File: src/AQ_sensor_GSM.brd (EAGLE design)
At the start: 110 x 64 mm, 51 parts, among them IC2 MCP73831/OT, J1 F-1X03-SIP-100-32, SW1 PCM12SMTR, SW2 PCM12SMTR, U2 TEXAS_INSTRUMENTS_SN74HC125TE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, U3 TEXAS_INSTRUMENTS_LM1117IMP-3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, U4 ESP8266-12E/ESP-12E, U5 CH340G, X1 53048-08, X2 SIMLOCK-C707_10M006_512_2, X4 50 Ohms

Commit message: Layout Update 2
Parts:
- moved POWER 107.0 mm to (9.54, 62.5)
- moved R14 103.9 mm to (7.71, 54.3), turned to 90 degrees
- moved C3 95.1 mm to (34.0, 54.8), turned to 90 degrees
- moved MICRO_USB 93.4 mm to (16.4, 60.0), turned to 180 degrees
- moved C2 87.8 mm to (34.0, 49.3), turned to 90 degrees
- moved R5 79.9 mm to (30.1, 14.7)
- moved J1 79.1 mm to (36.4, 14.2)
- moved R2 75.8 mm to (9.30, 59.5), turned to 270 degrees
- moved SW1 75.3 mm to (38.5, 59.0), turned to 90 degrees
- moved X1 61.1 mm to (35.5, 37.0), turned to 270 degrees
- moved C1 51.2 mm to (48.0, 34.4)
- moved Y1 35.1 mm to (30.2, 51.7), turned to 90 degrees
- moved U5 31.7 mm to (18.3, 51.4), turned to 270 degrees
- moved PMS 26.0 mm to (32.8, 28.0), turned to 270 degrees
- moved R4 23.8 mm to (30.2, 21.8)
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
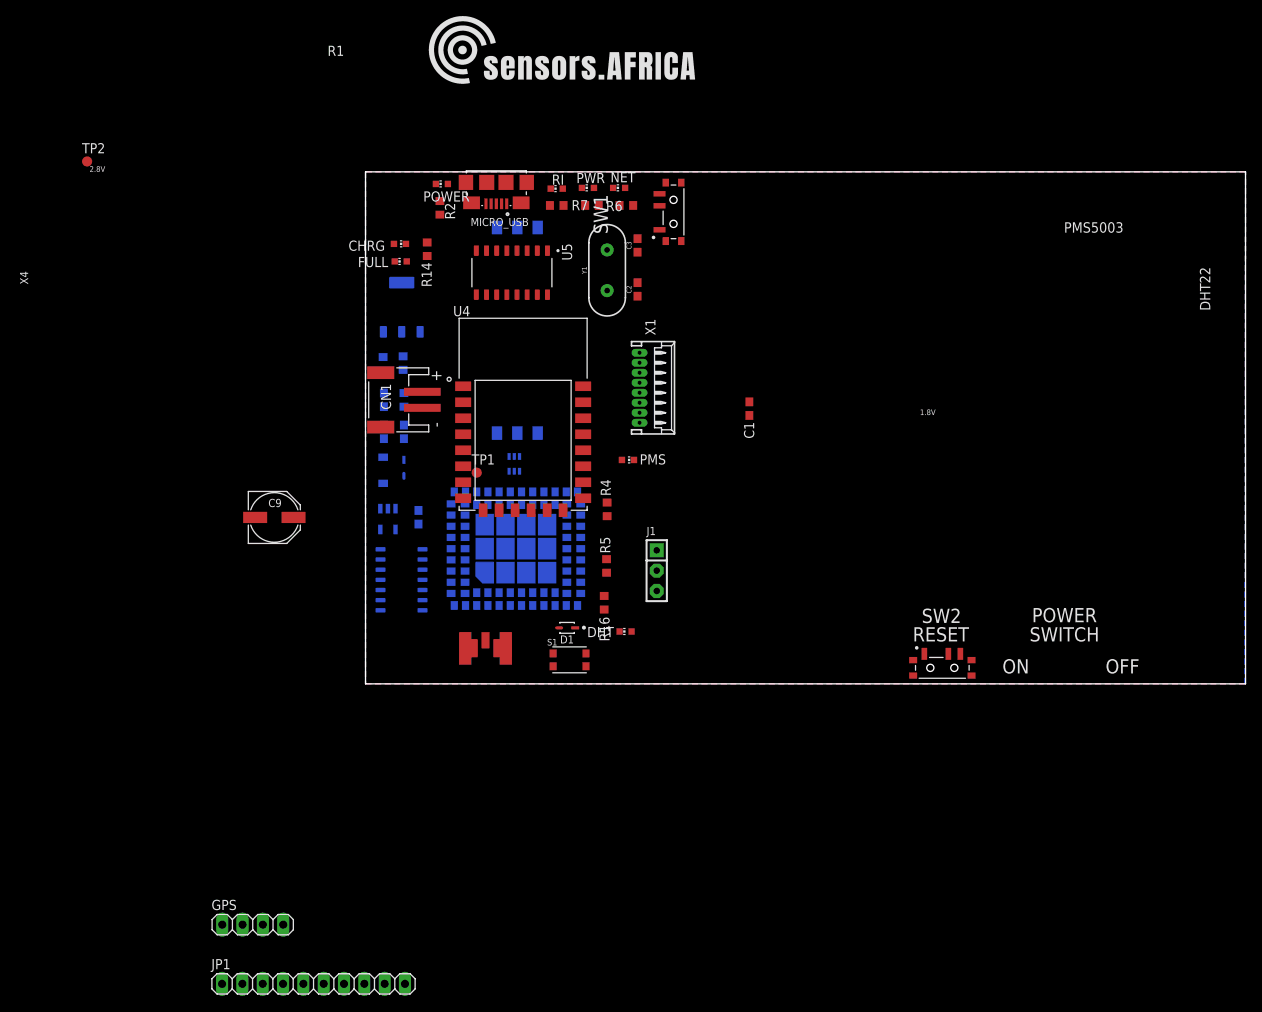
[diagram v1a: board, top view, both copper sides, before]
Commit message: PCB Resized
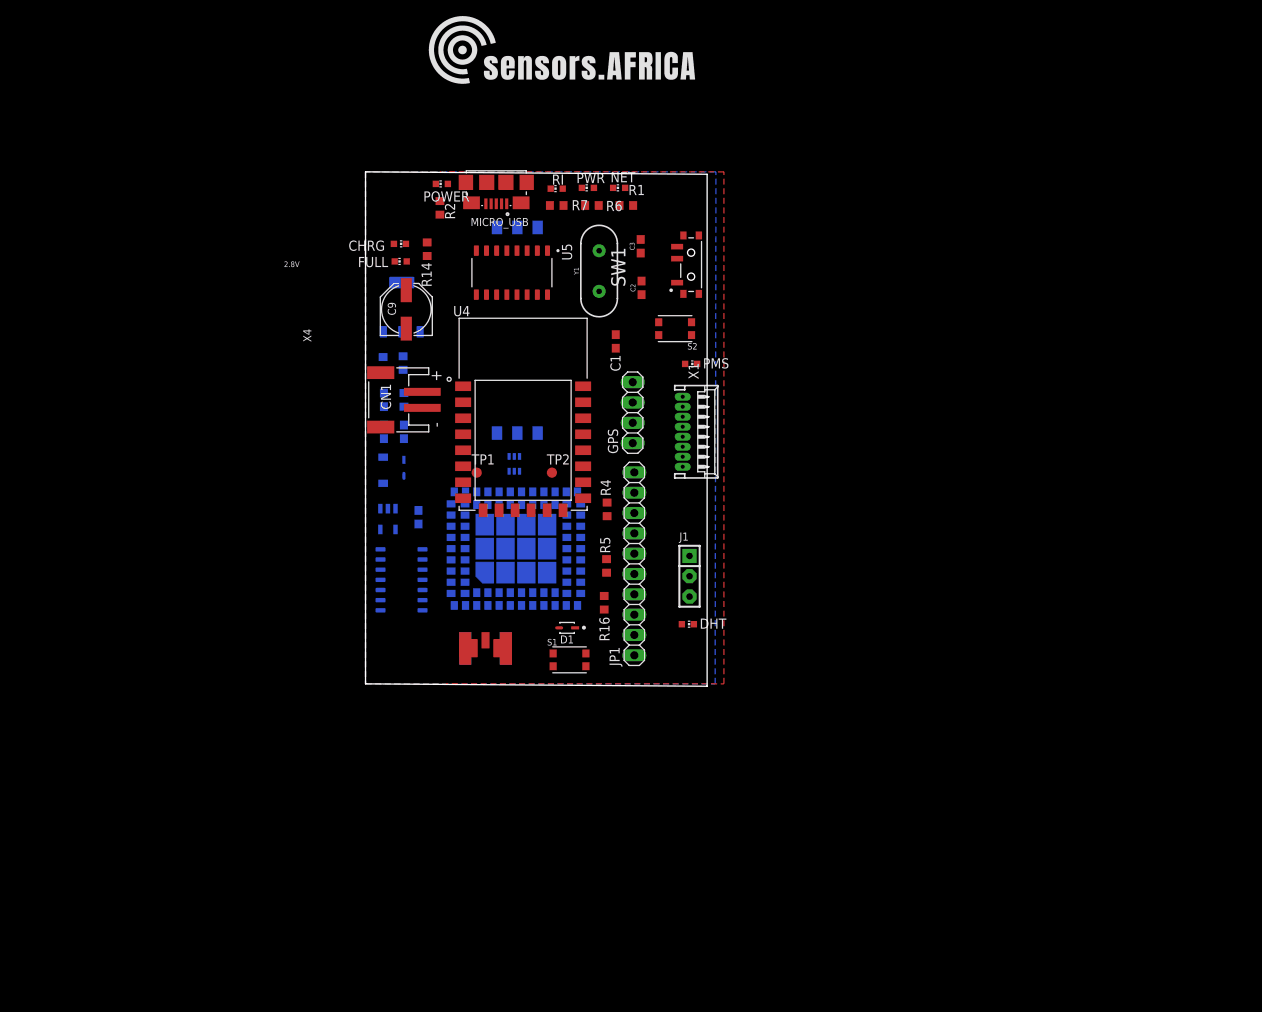
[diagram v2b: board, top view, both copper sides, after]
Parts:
- removed SW2: PCM12SMTR, AQ_sensor_GSM:SW_PCM12SMTR
- added S2: KMR621NGLFS, AQ_sensor_GSM:SW_KMR621NGLFS
- moved GPS 79.7 mm to (33.4, 33.9), turned to 90 degrees
- moved TP2 69.9 mm to (23.3, 26.4)
- moved JP1 66.1 mm to (33.6, 15.0), turned to 90 degrees
- moved C9 30.8 mm to (5.10, 46.8), turned to 90 degrees
- moved C1 18.7 mm to (31.3, 42.8)
- moved PMS 14.4 mm to (40.7, 40.0)
- moved DHT 7.84 mm to (40.3, 7.46), turned to 270 degrees
- moved X1 7.71 mm to (40.9, 31.5)
- moved SW1 6.96 mm to (40.7, 52.4)
- moved J1 4.16 mm to (40.5, 13.4)
- moved Y1 1.00 mm to (29.2, 51.6)
- moved C2 0.54 mm to (34.5, 49.5)
- moved C3 0.41 mm to (34.4, 54.7)
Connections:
- net ESP_RST: now also S2.1_1, S2.1_2; no longer SW2.2
- net GND: now also S2.2_1, S2.2_2; no longer SW2.1, SW2.S1, SW2.S2, SW2.S3, SW2.S4
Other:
- board size 110 x 64 mm -> 42.7 x 64.3 mm
- board text removed: "1.8V"
- board text removed: "DHT22"
- board text removed: "OFF"
- board text removed: "ON"
- board text removed: "PMS5003"
- board text removed: "POWER"
- board text removed: "RESET"
- board text removed: "SWITCH"

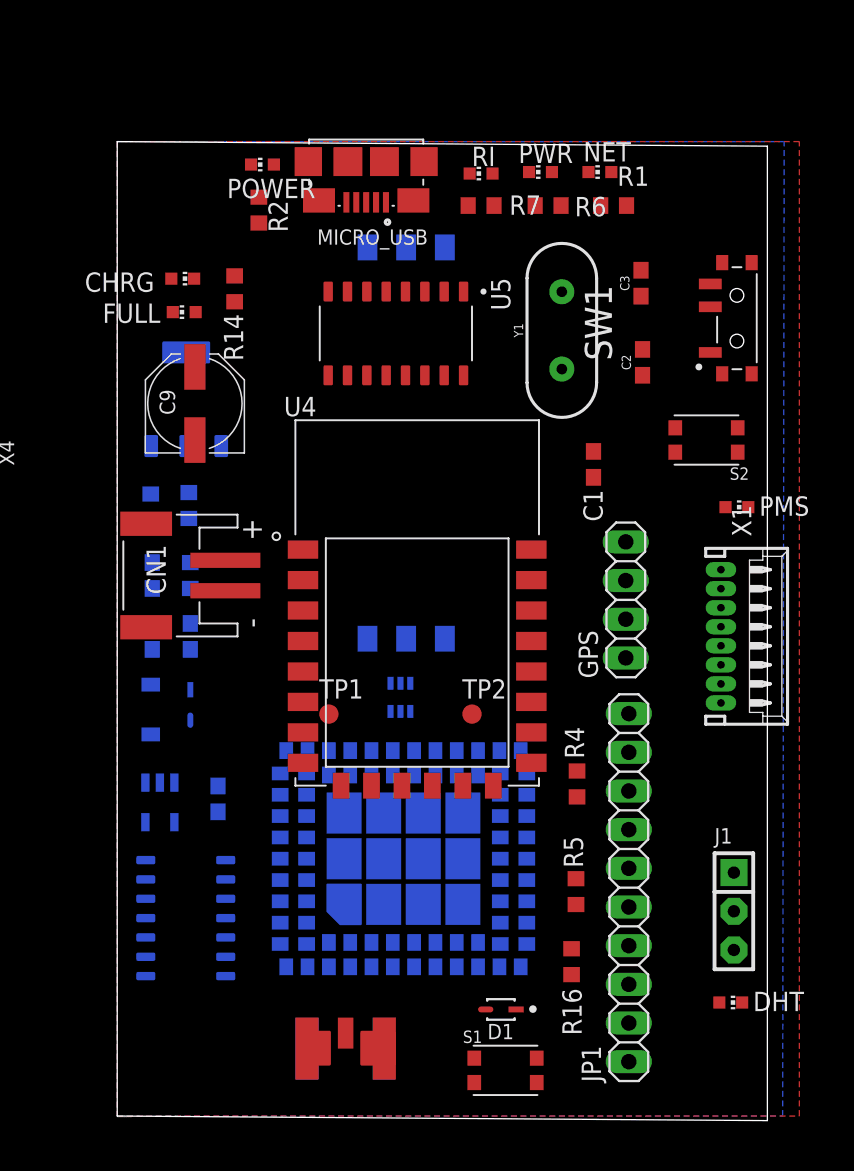
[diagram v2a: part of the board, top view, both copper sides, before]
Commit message: angle edges
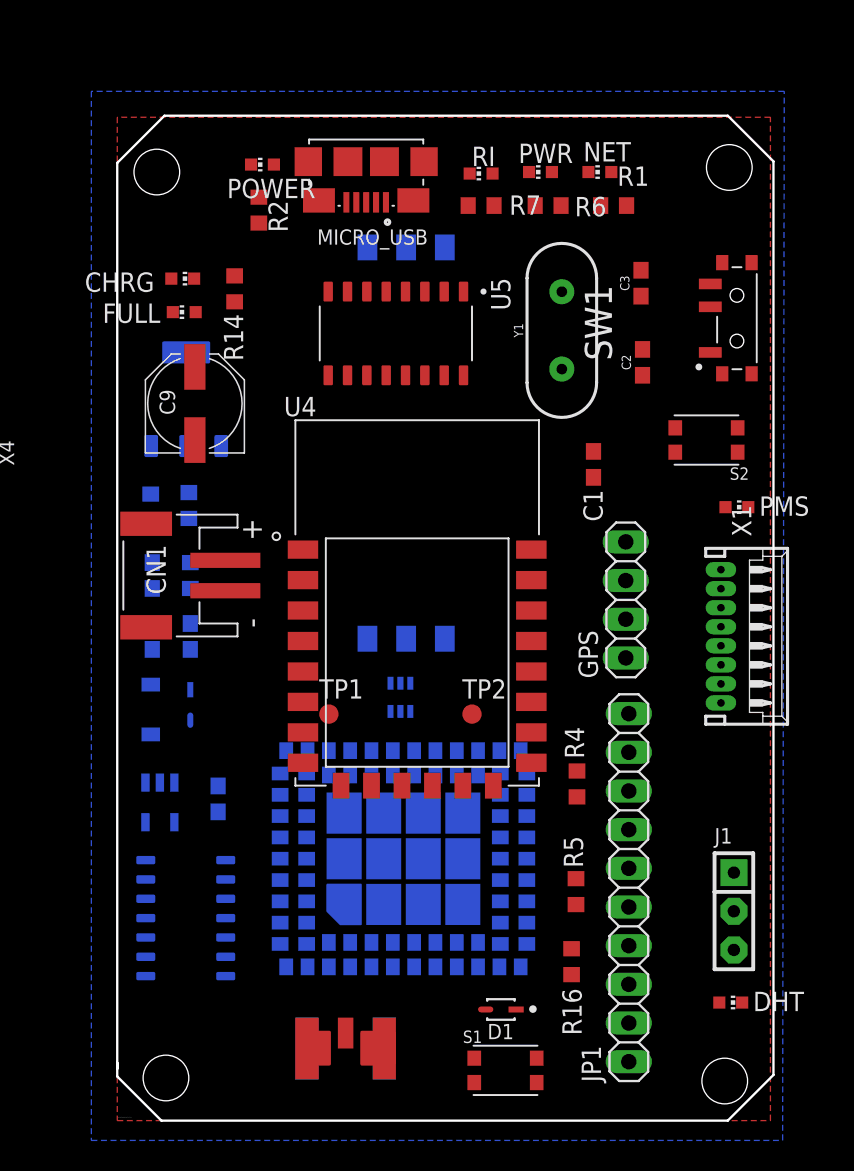
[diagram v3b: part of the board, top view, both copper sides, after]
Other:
- board size 42.7 x 64.3 mm -> 43.1 x 66 mm
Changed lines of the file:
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@@
 <fusionteam huburn="a.YnVzaW5lc3M6Y29kZWZvcmFmcmljYTE" projecturn="a.YnVzaW5lc3M6Y29kZWZvcmFmcmljYTEjMjAyMTEwMDU0NTIxNTU1MjY" folderUrn="urn:adsk.wipprod:fs.folder:co.V4eMQQrZRL-wTqnvGmJ6Nw" urn="urn:adsk.wipprod:dm.lineage:IWwQklixSQOxdVvh3w9Smg"  versionUrn="urn:adsk.wipprod:fs.file:vf.IWwQklixSQOxdVvh3w9Smg?version=1" camFileUrn="" camFileVersionUrn="" lastpublishedchangeguid="c8ef48bc-93d7-de42-14aa-f49d7ebfad5e"/>
 <plain>
-<wire x1="0" y1="0" x2="42.7" y2="-0.3" width="0" layer="20"/>
-<wire x1="42.7" y1="-0.3" x2="42.7" y2="63.7" width="0" layer="20"/>
-<wire x1="42.7" y1="63.7" x2="0" y2="64" width="0" layer="20"/>
-<wire x1="0" y1="64" x2="0" y2="0" width="0" layer="20"/>
 <text x="0" y="-0.0889" size="0.035559375" layer="21" font="vector">/Users/kirah/Downloads/Logo-Files-01.bmp</text>
 <dimension x1="0" y1="64" x2="110" y2="64" x3="55" y3="70.2" textsize="1.778" layer="25" dtype="horizontal"/>
@@
 <rectangle x1="11.748409375" y1="83.44585" x2="12.548509375" y2="83.463625" layer="21"/>
 <rectangle x1="12.08623125" y1="83.463628125" x2="12.22846875" y2="83.481409375" layer="21"/>
+<hole x="2.6" y="62" drill="3"/>
+<hole x="40.2" y="62.3" drill="3"/>
+<hole x="39.9" y="2.3" drill="3"/>
+<hole x="3.2" y="2.5" drill="3"/>
+<polygon width="0.1524" layer="20">
+<vertex x="0" y="3.1"/>
+<vertex x="0" y="62.6"/>
+<vertex x="3.1" y="65.7"/>
+<vertex x="40.1" y="65.7"/>
+<vertex x="43.1" y="62.7"/>
+<vertex x="43.1" y="2.7"/>
+<vertex x="40.1" y="-0.3"/>
+<vertex x="2.9" y="-0.3"/>
+<vertex x="0" y="2.6"/>
+<vertex x="0" y="3.5"/>
+</polygon>
 </plain>
 <attributes>
@@
 <contactref element="J1" pad="1"/>
 <polygon width="0.4" layer="1">
-<vertex x="0" y="0"/>
-<vertex x="44.8" y="0"/>
-<vertex x="44.8" y="64"/>
-<vertex x="0" y="64"/>
+<vertex x="0" y="-0.3"/>
+<vertex x="42.9" y="-0.3"/>
+<vertex x="42.9" y="65.6"/>
+<vertex x="0" y="65.6"/>
 </polygon>
 <polygon width="0.4" layer="16">
-<vertex x="0" y="0"/>
-<vertex x="43.70390625" y="0"/>
-<vertex x="43.80390625" y="64"/>
-<vertex x="0" y="64"/>
+<vertex x="-1.7" y="-1.6"/>
+<vertex x="43.70140625" y="-1.6"/>
+<vertex x="43.8090625" y="67.3"/>
+<vertex x="-1.7" y="67.3"/>
 </polygon>
 <contactref element="POWER" pad="C"/>

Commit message: Curved Board edges
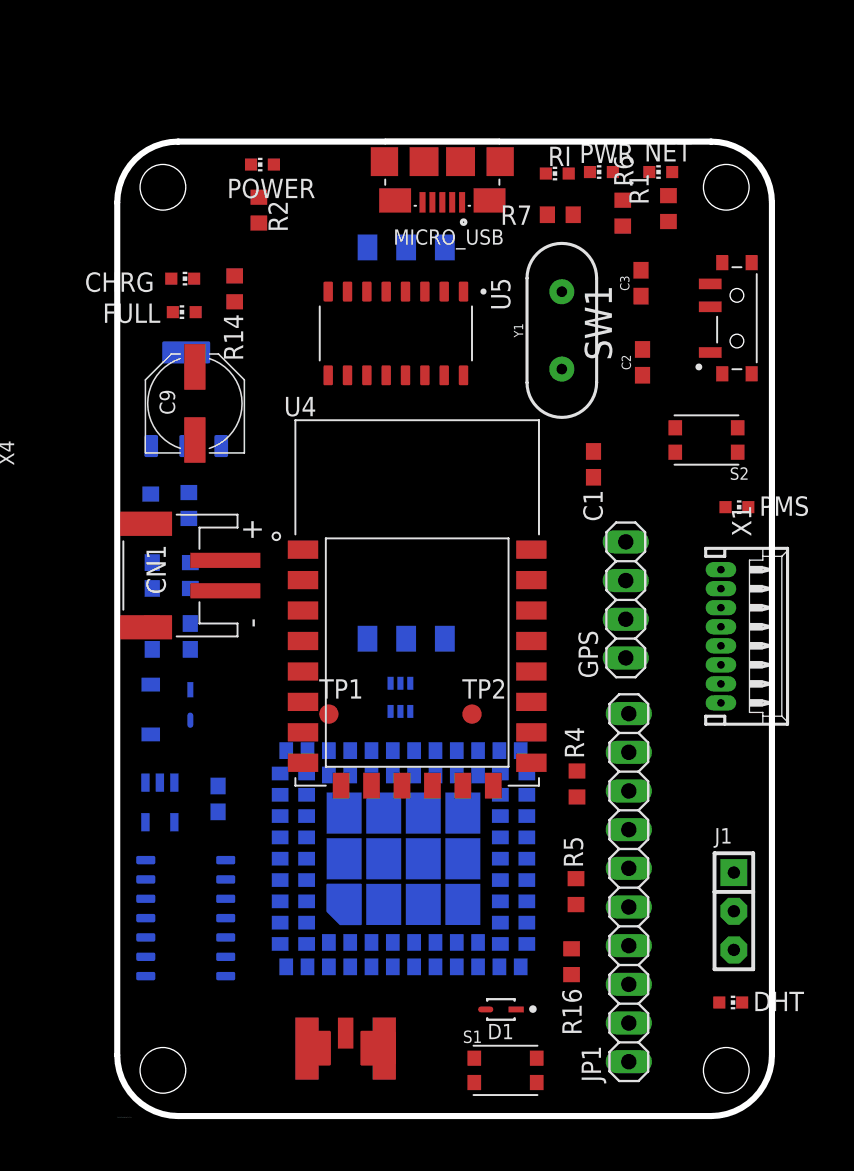
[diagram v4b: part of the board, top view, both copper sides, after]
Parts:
- moved R7 5.23 mm to (29.1, 59.2), turned to 0 degrees
- moved MICRO_USB 5.00 mm to (21.4, 60.0)
- moved RI 5.00 mm to (28.9, 61.9)
- moved R6 4.93 mm to (33.2, 59.3), turned to 270 degrees
- moved NET 4.00 mm to (35.7, 62.0)
- moved PWR 4.00 mm to (31.8, 62.0)
- moved R1 3.61 mm to (36.2, 59.6), turned to 270 degrees
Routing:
- removed copper zone on layer 1, net GND
- removed copper zone on layer 16, net GND
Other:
- board size 43.1 x 66 mm -> 43 x 64 mm

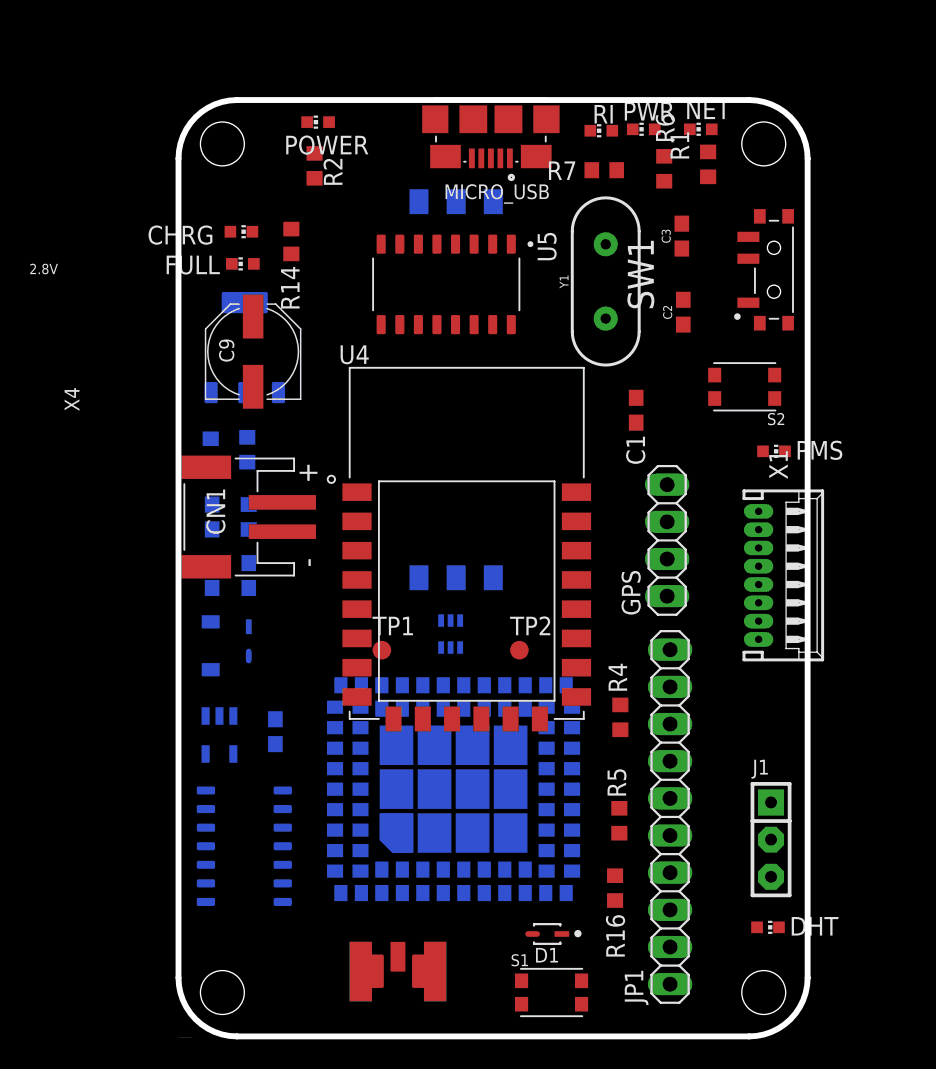
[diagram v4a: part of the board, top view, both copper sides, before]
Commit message: Curved Board edges
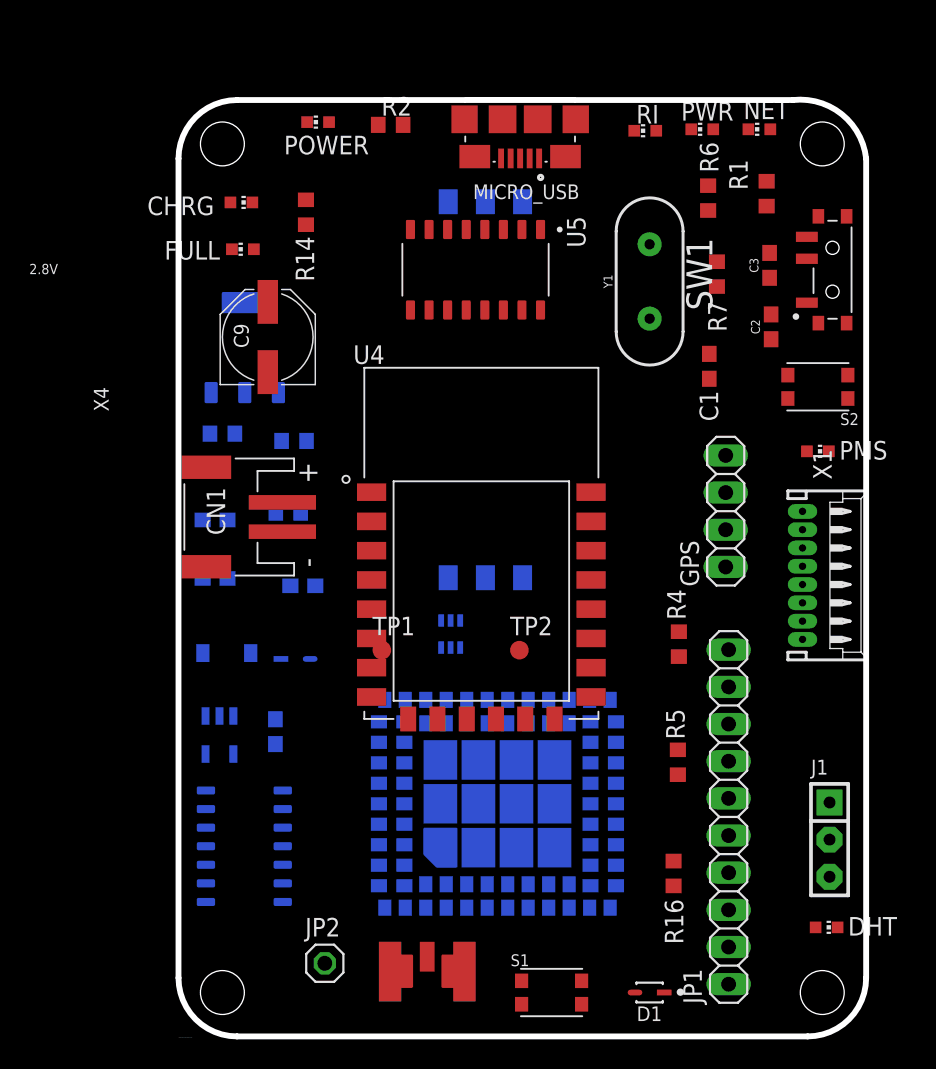
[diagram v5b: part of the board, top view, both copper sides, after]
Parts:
- added JP2: PINHD-1X1, Connector:1X01
- moved R7 10.5 mm to (36.8, 52.1), turned to 90 degrees
- moved D1 8.06 mm to (32.2, 3.00)
- moved R4 6.40 mm to (34.2, 26.8)
- moved C3 6.32 mm to (40.4, 52.7)
- moved C2 6.08 mm to (40.5, 48.5)
- moved R2 5.91 mm to (14.5, 62.3), turned to 0 degrees
- moved C1 5.83 mm to (36.3, 45.8)
- moved R5 5.66 mm to (34.1, 18.7)
- moved S2 5.00 mm to (43.7, 44.4)
- moved GPS 4.47 mm to (37.4, 35.9)
- moved R1 4.47 mm to (40.2, 57.6)
- moved R16 4.12 mm to (33.8, 11.1)
- moved DHT 4.00 mm to (44.3, 7.46)
- moved J1 4.00 mm to (44.5, 13.4)
- moved JP1 4.00 mm to (37.6, 15.0)
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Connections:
- net GSM_ANT: now also JP2.1
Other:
- board size 43 x 64 mm -> 47 x 64 mm

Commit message: Components Allignment
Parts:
- moved IC2 16.2 mm to (17.8, 26.6)
- moved D3 13.0 mm to (31.6, 27.5)
- moved TP2 11.2 mm to (13.3, 31.4)
- moved U3 7.21 mm to (8.53, 53.1)
- moved X2 5.83 mm to (24.6, 47.2)
- moved U4 5.66 mm to (24.7, 26.2)
- moved D4 5.28 mm to (10.2, 21.0), turned to 90 degrees
- moved R14 5.00 mm to (13.7, 56.3)
- moved D2 4.93 mm to (2.80, 21.3), turned to 90 degrees
- moved FULL 4.92 mm to (2.20, 49.4), turned to 180 degrees
- moved R4 4.65 mm to (38.2, 29.2), turned to 180 degrees
- moved C2 4.47 mm to (38.5, 44.5), turned to 180 degrees
- moved U2 4.30 mm to (8.00, 10.5), turned to 90 degrees
- moved X4 4.12 mm to (21.0, 1.40)
- moved S1 4.00 mm to (29.5, 3.00)
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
